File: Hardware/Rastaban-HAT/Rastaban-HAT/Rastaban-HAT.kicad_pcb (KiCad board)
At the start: 4 copper layers, 68.7 x 65.4 mm, 86 parts, among them IC2 BCM53DS, J1 1778780, J10 GPIO, J11 Conn_01x06_Male, J2 1778780, J3 1778780, J4 Screw_Terminal_01x02, J5 Jack-DC 12V+, J6 SM04B-SRSS-TB(LF)(SN), J7 Screw_Terminal_01x02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

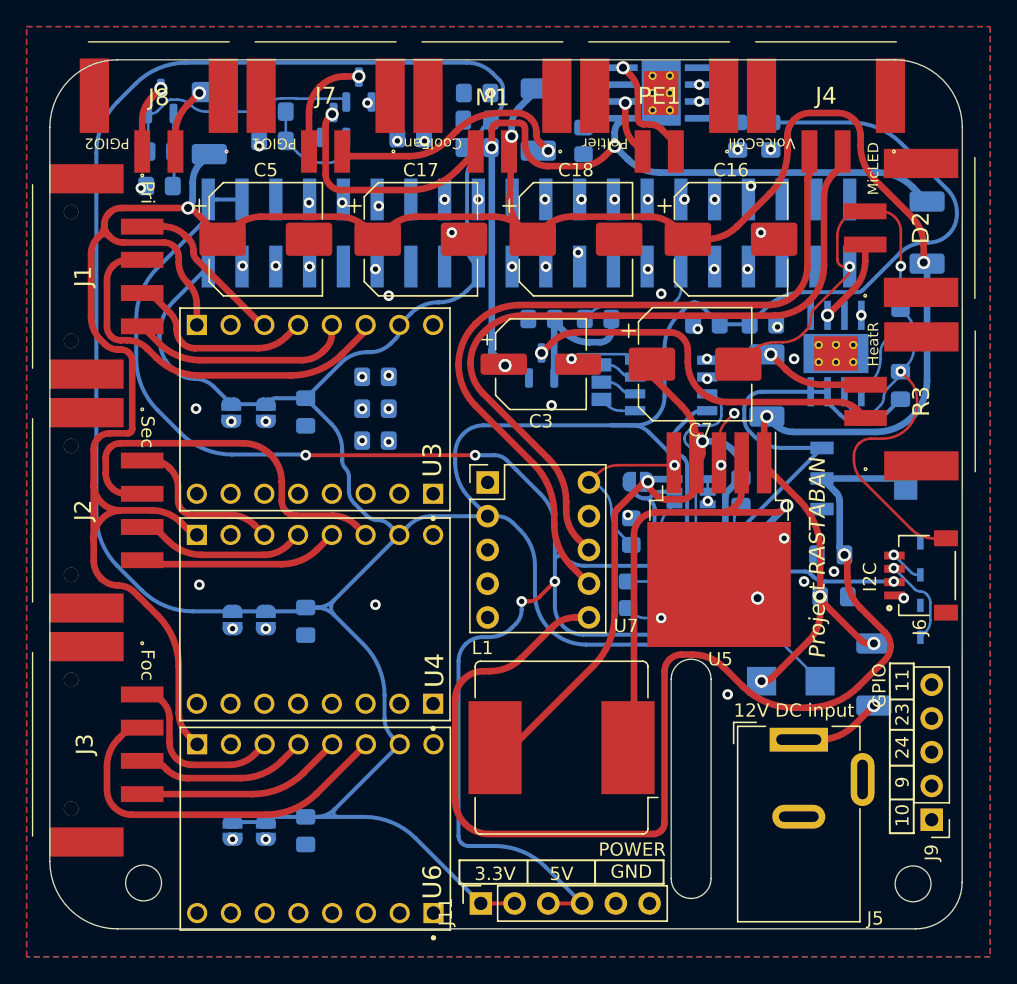
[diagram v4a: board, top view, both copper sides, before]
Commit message: worked on PCB and schematic designs
many small changes and some big schematic changes (motors)
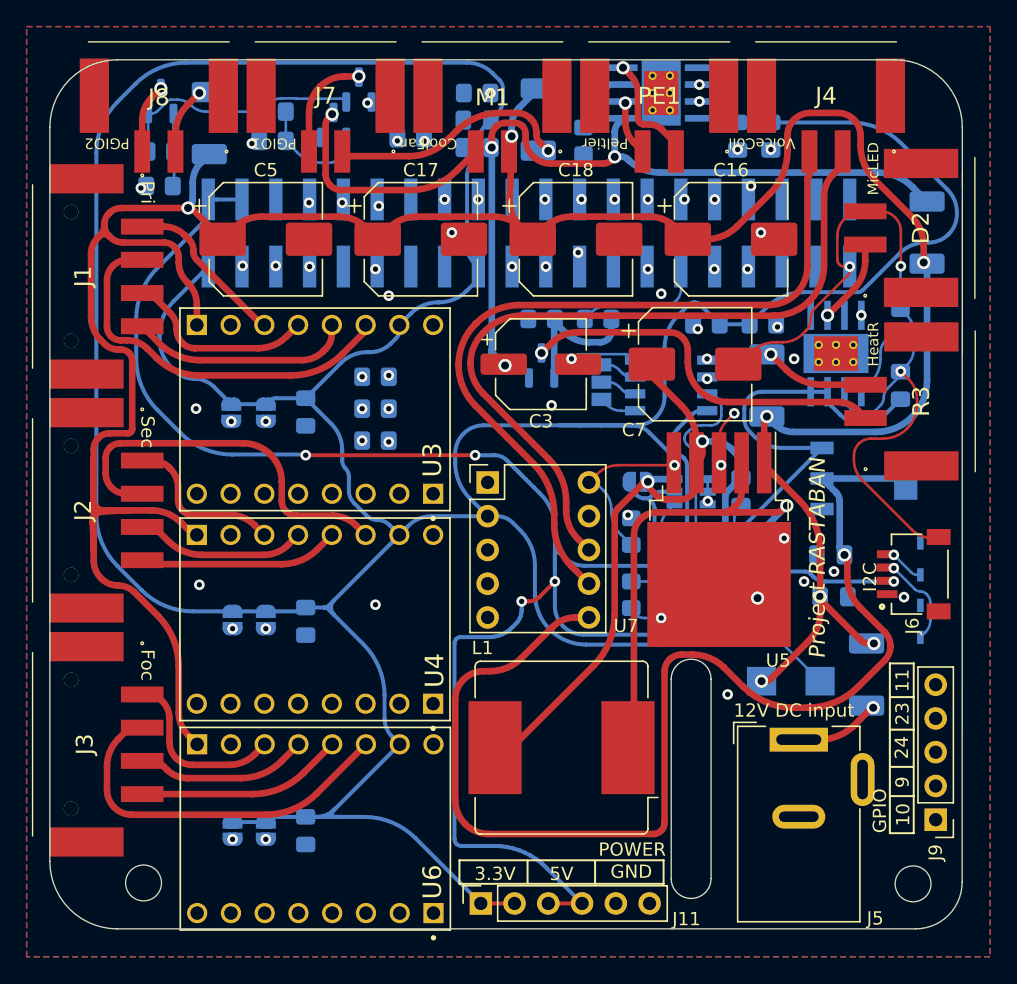
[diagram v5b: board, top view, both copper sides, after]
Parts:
- moved J6 0.56 mm to (157.2, 106.2)
- moved J9 0.55 mm to (155.7, 113.8)
- moved J9 0.30 mm to (160.9, 124.7)
- moved R12 0.25 mm to (138.0, 107.8)
- renumbered 11 to J9
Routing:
- net 3.3V+: track 348.3 -> 352.9 mm
- net 12V+: track 220.1 -> 224.6 mm
- net 5V+: track 169.7 -> 172.2 mm
- net GPIO23: track 58.5 -> 59.6 mm
- net RX: track 68.0 -> 68.9 mm
- net CTRLFAN: track 42.2 -> 41.6 mm
- net Net-(C2-Pad2): track 57.7 -> 57.2 mm
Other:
- board text added: "Project: Rastaban Version: 0.3 Date: 13-12-2022 Designed by: Casper R. Tak"
- board text added: "UART set R."
- board text removed: "Project: Rastaban Version: 0.3 Date: 08-12-2022 Designed by: Casper R. Tak"

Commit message: tmc2209 pinout changed (moved RX)
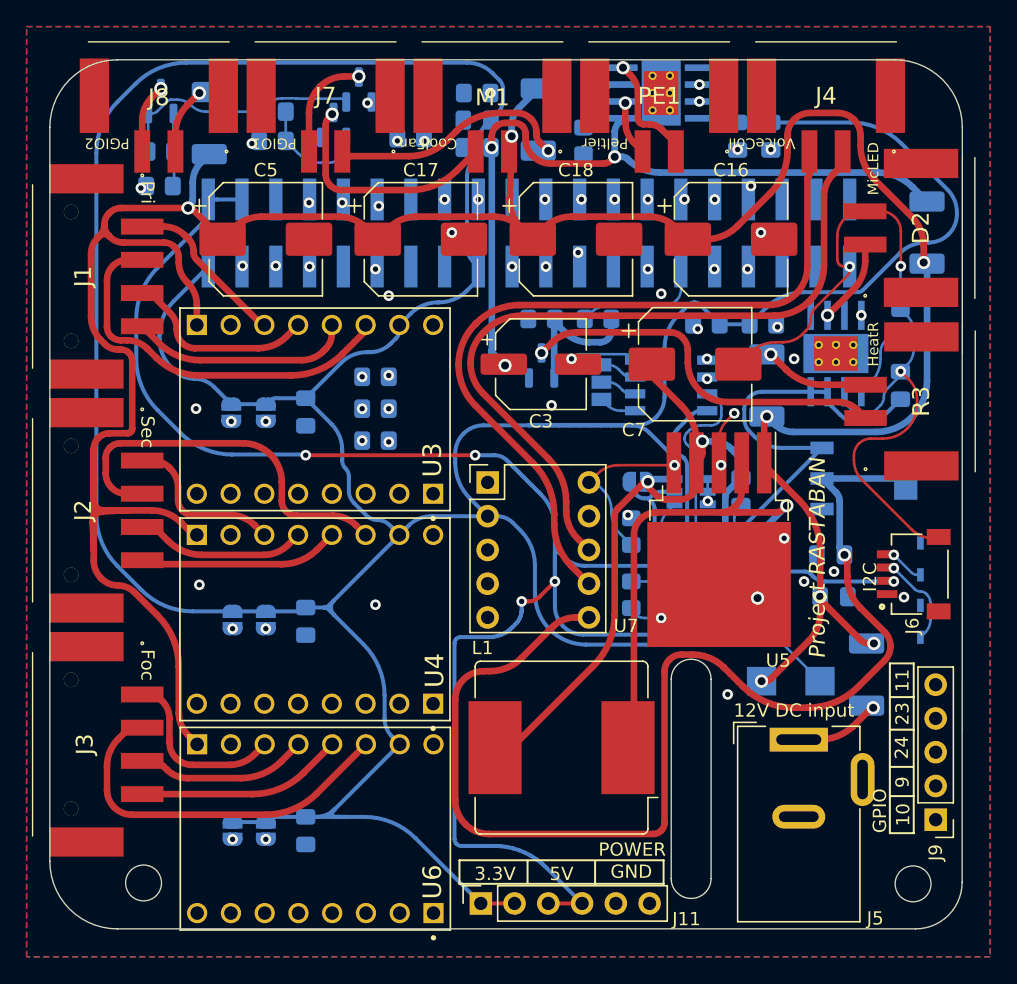
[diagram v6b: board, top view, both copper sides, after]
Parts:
- renumbered J9 to F1
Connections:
- U3 pad JP1_3: RX -> unconnected-(U3-PadJP1_3)
- U3 pad JP1_4: unconnected-(U3-PadJP1_4) -> RX
- U4 pad JP1_3: RX -> unconnected-(U4-PadJP1_3)
- U4 pad JP1_4: unconnected-(U4-PadJP1_4) -> RX
- U6 pad JP1_3: RX -> unconnected-(U6-PadJP1_3)
- U6 pad JP1_4: unconnected-(U6-PadJP1_4) -> RX
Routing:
- net RX: track 68.9 -> 65.9 mm
- net 3.3V+: track 352.9 -> 355.5 mm
- net unconnected-(U3-PadJP1_3): track 0.00 -> 2.12 mm
- net GPIO23: track 59.6 -> 58.3 mm
- net 5V+: track 172.2 -> 172.9 mm
- net 12V+: track 224.6 -> 225.2 mm
- net GPIO11: track 45.5 -> 44.8 mm

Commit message: added enable pins back for tmc drivers
they are required for uart control
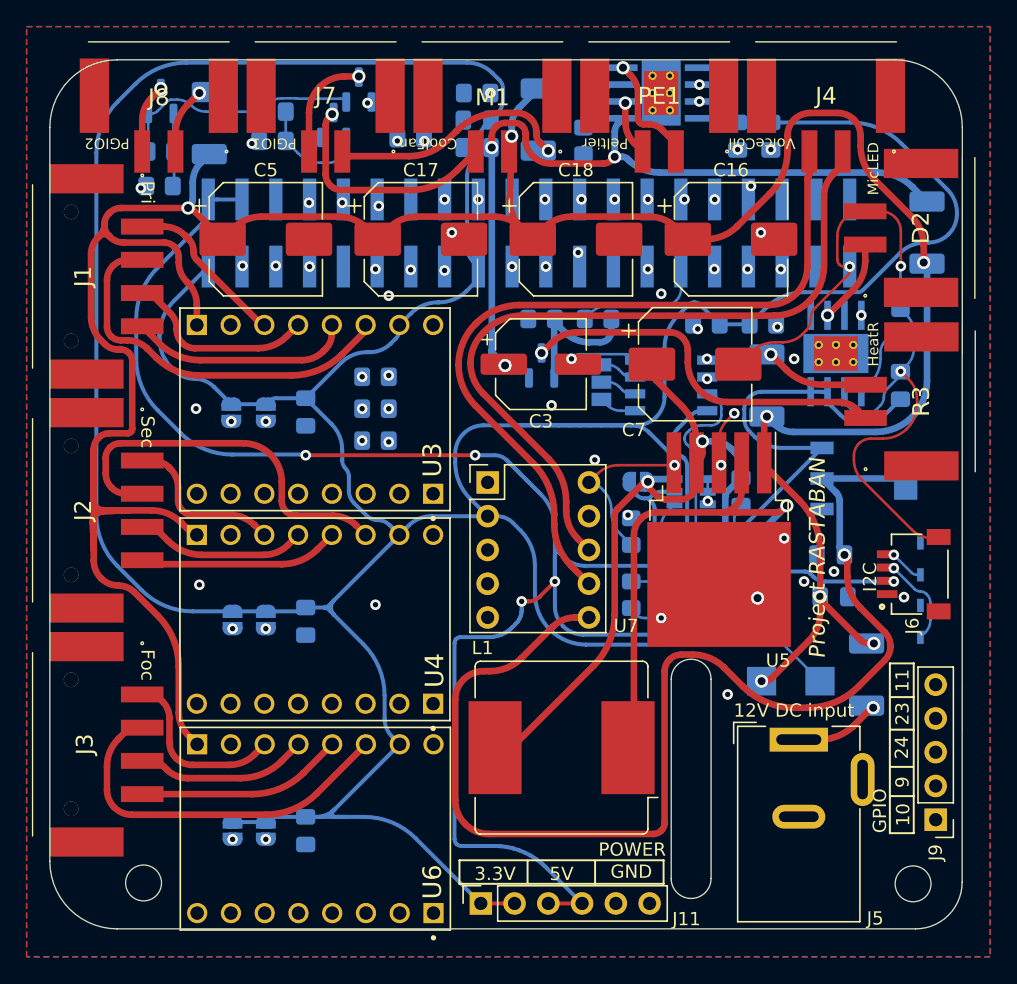
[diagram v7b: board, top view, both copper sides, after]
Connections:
- J10 pad 14: unconnected-(J10-Pad14) -> EnaPri
- J10 pad 16: unconnected-(J10-Pad16) -> EnaSec
- J10 pad 36: unconnected-(J10-Pad36) -> EnaFoc
- U3 pad JP1_8: unconnected-(U3-PadJP1_8) -> EnaPri
- U4 pad JP1_8: unconnected-(U4-PadJP1_8) -> EnaSec
- U6 pad JP1_8: unconnected-(U6-PadJP1_8) -> EnaFoc
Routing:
- net EnaFoc: track 0.00 -> 101.1 mm, vias 0 -> 2
- net EnaSec: track 0.00 -> 56.4 mm, vias 0 -> 1
- net EnaPri: track 0.00 -> 35.9 mm, vias 0 -> 1
- net 3.3V+: track 355.5 -> 356.4 mm

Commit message: added back B-EMF diodes to PGIO's
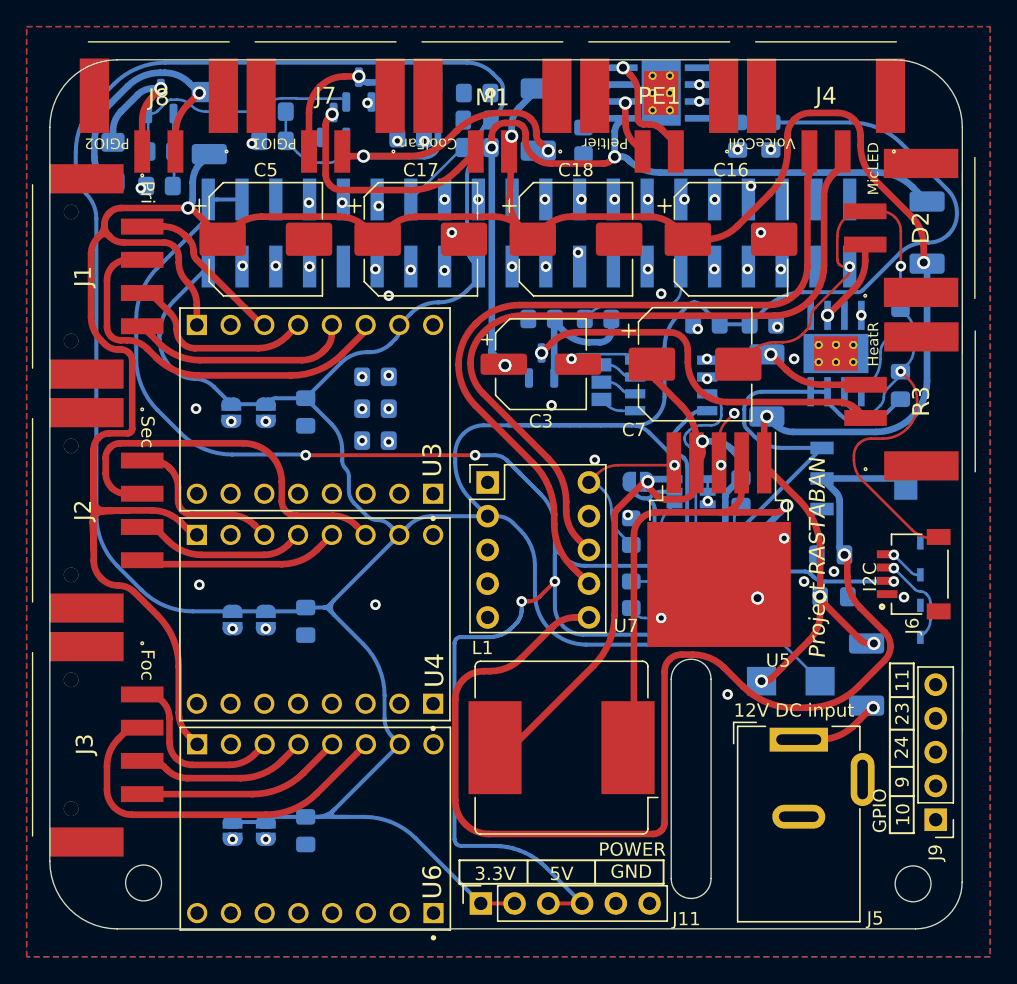
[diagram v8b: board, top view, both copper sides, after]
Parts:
- added D6: DIODE-1N4148, Diode_SMD:D_1206_3216Metric_Pad1.42x1.75mm_HandSolder, B.Cu at (121.6, 69.2)
- added D7: DIODE-1N4148, Diode_SMD:D_1206_3216Metric_Pad1.42x1.75mm_HandSolder, B.Cu at (99.0, 75.2)
- F2, F3: value 2A -> 3A
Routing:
- net Net-(F3-Pad2): track 5.00 -> 19.8 mm
- net Net-(F2-Pad2): track 18.2 -> 29.0 mm, vias 1 -> 2
- net Net-(J8-Pad2): track 5.20 -> 11.3 mm
- net GND: track 123.7 -> 129.2 mm
- net 3.3V+: track 356.4 -> 359.2 mm
- net Net-(J7-Pad2): track 8.21 -> 11.0 mm
